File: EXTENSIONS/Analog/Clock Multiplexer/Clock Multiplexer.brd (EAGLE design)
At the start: 47 x 71 mm, 9 parts

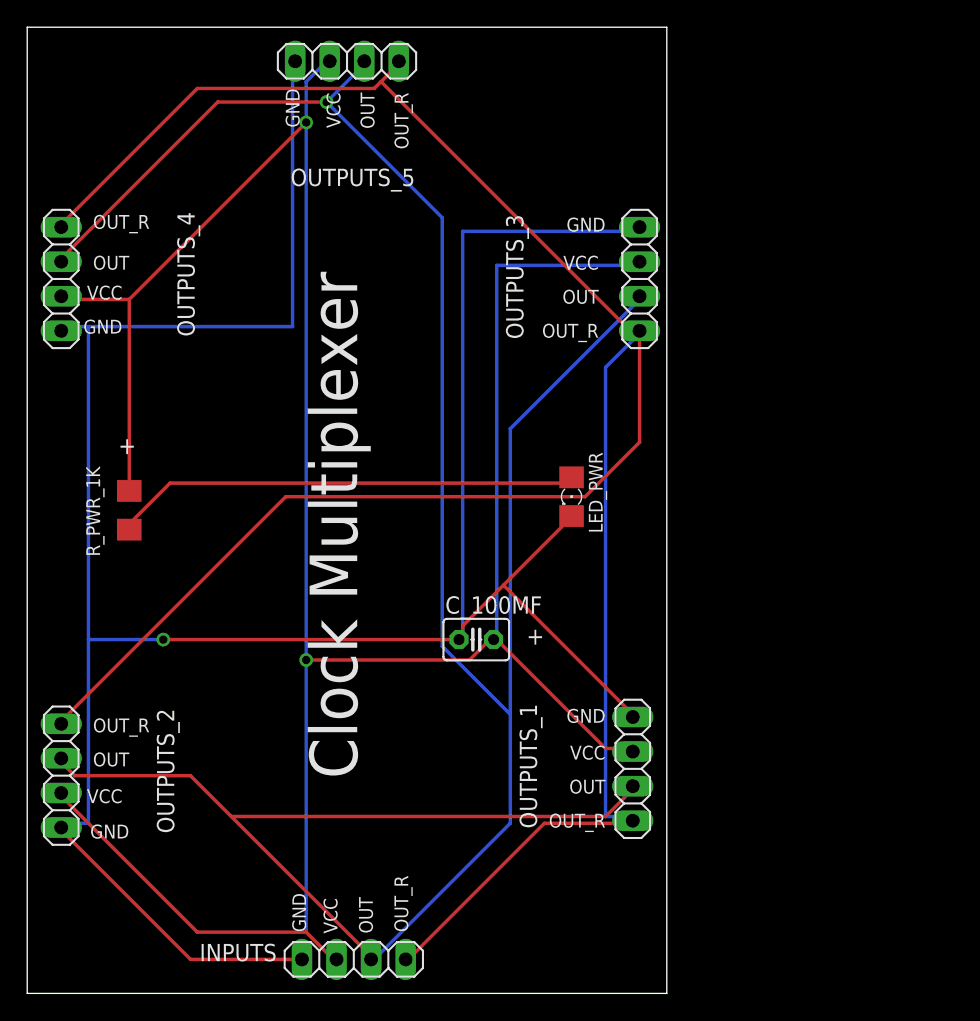
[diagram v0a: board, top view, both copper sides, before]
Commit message: update clock multiplexer
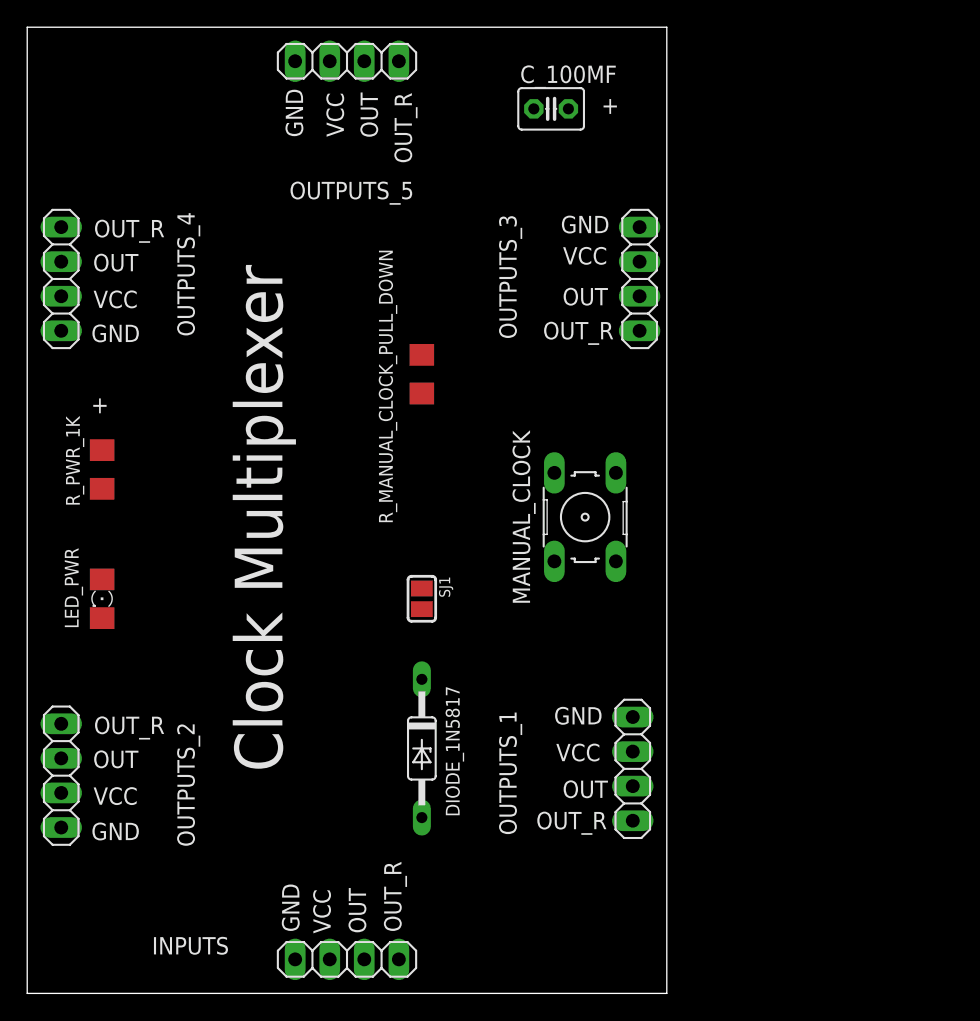
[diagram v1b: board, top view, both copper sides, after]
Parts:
- added DIODE_1N5817: 1N821, diode:DO35Z10
- added MANUAL_CLOCK: (no value), switch-omron:B3F-10XX
- added R_MANUAL_CLOCK_PULL_DOWN: (no value), adafruit:R1206
- added SJ1: (no value), microbuilder:SOLDERJUMPER_REFLOW
- moved C_100MF 39.4 mm to (40.5, 77.0)
- moved LED_PWR 35.3 mm to (7.50, 41.0)
- moved R_PWR_1K 3.61 mm to (7.50, 50.5)
- moved JP_CLOCK_IN 0.50 mm to (25.5, 14.5)
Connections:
- new net N$2: DIODE_1N5817.C, SJ1.2
- new net TMR555_OUTPUT_2: MANUAL_CLOCK.4, OUTPUTS_1.3, OUTPUTS_2.3, OUTPUTS_3.3, OUTPUTS_4.3, OUTPUTS_5.3, R_MANUAL_CLOCK_PULL_DOWN.2, SJ1.1
- net GND: now also R_MANUAL_CLOCK_PULL_DOWN.1
- net TMR555_OUTPUT: now also DIODE_1N5817.A; no longer OUTPUTS_1.3, OUTPUTS_2.3, OUTPUTS_3.3, OUTPUTS_4.3, OUTPUTS_5.3
- net VCC: now also MANUAL_CLOCK.1
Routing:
- net VCC: track 197.7 -> 0.00 mm, vias 2 -> 0
- net TMR555_OUTPUT: track 196.5 -> 0.00 mm, vias 1 -> 0
- net GND: track 194.7 -> 0.00 mm, vias 1 -> 0
- net TMR555_OUTPUT_REVERSE: track 176.5 -> 0.00 mm
- net N$1: track 34.6 -> 0.00 mm
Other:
- board text added: "PCBv1 - 2019.10"
- board text removed: "PCBv1 - 2019.09"

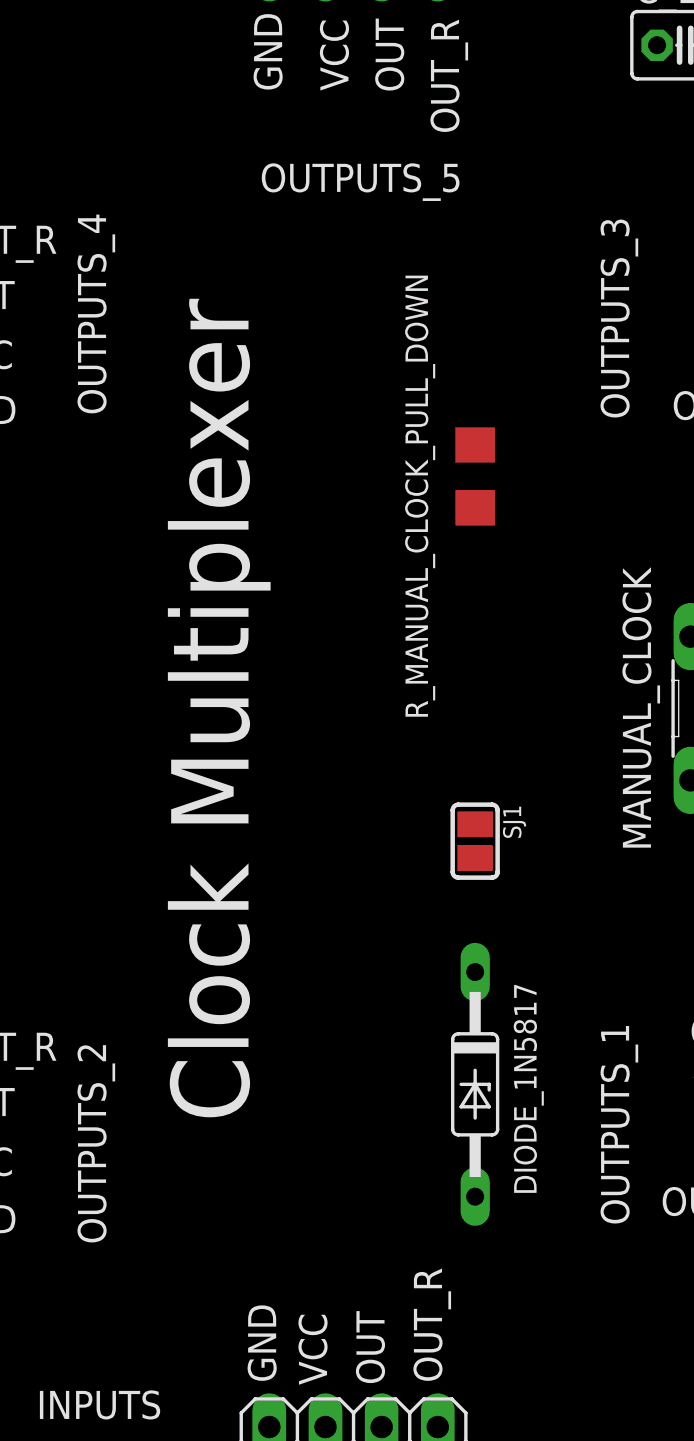
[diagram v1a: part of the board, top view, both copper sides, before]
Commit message: update clock multiplexer
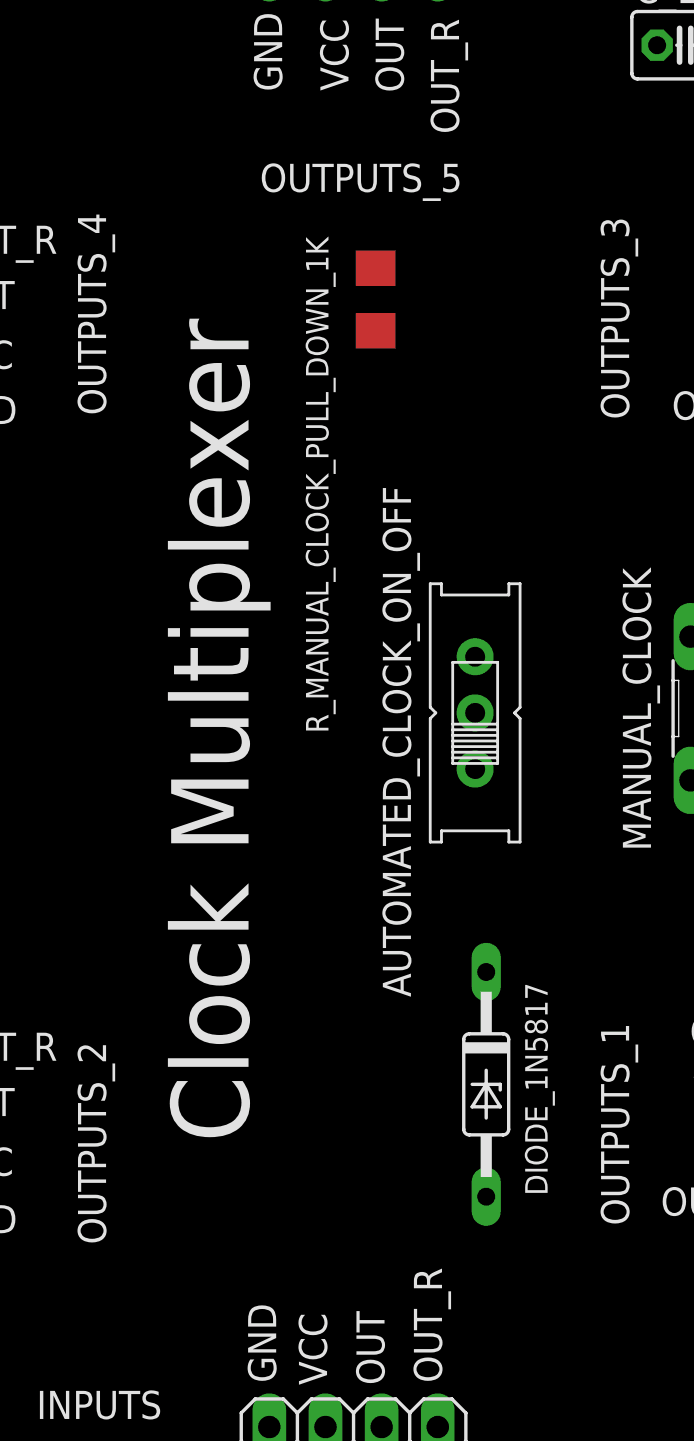
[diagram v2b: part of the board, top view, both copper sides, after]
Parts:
- removed R_MANUAL_CLOCK_PULL_DOWN: (no value), adafruit:R1206
- removed SJ1: (no value), microbuilder:SOLDERJUMPER_REFLOW
- added AUTOMATED_CLOCK_ON_OFF: (no value), adafruit:EG1218
- added R_MANUAL_CLOCK_PULL_DOWN_1K: (no value), adafruit:R1206
- moved DIODE_1N5817 0.50 mm to (31.5, 30.0)
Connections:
- net GND: now also R_MANUAL_CLOCK_PULL_DOWN_1K.1; no longer R_MANUAL_CLOCK_PULL_DOWN.1
- net N$2: now also AUTOMATED_CLOCK_ON_OFF.P; no longer SJ1.2
- net TMR555_OUTPUT_2: now also AUTOMATED_CLOCK_ON_OFF.O, R_MANUAL_CLOCK_PULL_DOWN_1K.2; no longer R_MANUAL_CLOCK_PULL_DOWN.2, SJ1.1
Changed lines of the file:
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@@
 <text x="42" y="24.7" size="1.27" layer="25" rot="R180" align="center">OUT_R</text>
 <text x="27.5" y="21" size="1.27" layer="26" rot="MR0" align="center">PCBv1 - 2019.10</text>
-<text x="19" y="46.9" size="3.5" layer="25" rot="R270" align="center">Clock Multiplexer</text>
+<text x="19" y="46" size="3.5" layer="25" rot="R270" align="center">Clock Multiplexer</text>
 <text x="14" y="15.5" size="1.27" layer="25" rot="R180" align="center">INPUTS</text>
 <text x="27" y="48" size="3.5" layer="26" rot="MR90" align="center">MadeInTheUSB.net</text>
@@
 <attribute name="VALUE" x="48.08" y="43.952" size="1.27" layer="27" ratio="10" rot="R90"/>
 </element>
-<element name="R_MANUAL_CLOCK_PULL_DOWN" library="adafruit" package="R1206" value="" x="31" y="57.5" smashed="yes" rot="R90">
-<attribute name="NAME" x="28.357" y="56.603" size="1.016" layer="25" rot="R90" align="center"/>
-<attribute name="VALUE" x="33.413" y="56.103" size="1.27" layer="27" rot="R90"/>
-</element>
-<element name="SJ1" library="microbuilder" package="SOLDERJUMPER_REFLOW" value="" x="31" y="41" rot="R270"/>
-<element name="DIODE_1N5817" library="diode" package="DO35Z10" value="1N821" x="31" y="30" smashed="yes" rot="R270">
-<attribute name="NAME" x="33.27" y="29.786" size="1.016" layer="25" ratio="10" rot="R270" align="center"/>
-<attribute name="VALUE" x="28.46" y="32.286" size="1.27" layer="27" ratio="10" rot="R270"/>
+<element name="R_MANUAL_CLOCK_PULL_DOWN_1K" library="adafruit" package="R1206" value="" x="26.5" y="65.5" smashed="yes" rot="R90">
+<attribute name="NAME" x="23.857" y="57.103" size="1.016" layer="25" rot="R90" align="center"/>
+<attribute name="VALUE" x="28.913" y="64.103" size="1.27" layer="27" rot="R90"/>
+</element>
+<element name="DIODE_1N5817" library="diode" package="DO35Z10" value="1N821" x="31.5" y="30" smashed="yes" rot="R270">
+<attribute name="NAME" x="33.77" y="29.786" size="1.016" layer="25" ratio="10" rot="R270" align="center"/>
+<attribute name="VALUE" x="28.96" y="32.286" size="1.27" layer="27" ratio="10" rot="R270"/>
+</element>
+<element name="AUTOMATED_CLOCK_ON_OFF" library="adafruit" package="EG1218" value="" x="31" y="46.8" smashed="yes" rot="R90">
+<attribute name="NAME" x="27.46" y="45.506" size="1.27" layer="25" font="vector" rot="R90" align="center"/>
 </element>
 </elements>
@@
 <contactref element="OUTPUTS_5" pad="1"/>
 <contactref element="C_100MF" pad="1"/>
-<contactref element="R_MANUAL_CLOCK_PULL_DOWN" pad="1"/>
+<contactref element="R_MANUAL_CLOCK_PULL_DOWN_1K" pad="1"/>
 <wire x1="47" y1="68.31" x2="39.23" y2="77" width="0" layer="19" extent="1-1"/>
-<wire x1="21.69" y1="80.5" x2="39.23" y2="77" width="0" layer="19" extent="1-1"/>
-<wire x1="4.5" y1="60.69" x2="21.69" y2="80.5" width="0" layer="19" extent="1-1"/>
+<wire x1="26.5" y1="64.078" x2="39.23" y2="77" width="0" layer="19" extent="1-1"/>
+<wire x1="21.69" y1="80.5" x2="26.5" y2="64.078" width="0" layer="19" extent="1-1"/>
+<wire x1="4.5" y1="60.69" x2="26.5" y2="64.078" width="0" layer="19" extent="1-1"/>
 <wire x1="7.5" y1="39.578" x2="4.5" y2="60.69" width="0" layer="19" extent="1-1"/>
 <wire x1="4.5" y1="24.19" x2="7.5" y2="39.578" width="0" layer="19" extent="1-1"/>
 <wire x1="21.69" y1="14.5" x2="4.5" y2="24.19" width="0" layer="19" extent="1-1"/>
-<wire x1="31" y1="56.078" x2="7.5" y2="39.578" width="0" layer="19" extent="1-1"/>
-<wire x1="46.5" y1="32.31" x2="31" y2="56.078" width="0" layer="19" extent="1-1"/>
+<wire x1="46.5" y1="32.31" x2="21.69" y2="14.5" width="0" layer="19" extent="1-1"/>
 </signal>
 <signal name="VCC">
@@
 <contactref element="JP_CLOCK_IN" pad="3"/>
 <contactref element="DIODE_1N5817" pad="A"/>
-<wire x1="26.77" y1="14.5" x2="31" y2="24.92" width="0" layer="19" extent="1-1"/>
+<wire x1="26.77" y1="14.5" x2="31.5" y2="24.92" width="0" layer="19" extent="1-1"/>
 </signal>
 <signal name="TMR555_OUTPUT_REVERSE">
@@
 <contactref element="OUTPUTS_4" pad="3"/>
 <contactref element="MANUAL_CLOCK" pad="4"/>
-<contactref element="R_MANUAL_CLOCK_PULL_DOWN" pad="2"/>
-<contactref element="SJ1" pad="1"/>
+<contactref element="R_MANUAL_CLOCK_PULL_DOWN_1K" pad="2"/>
+<contactref element="AUTOMATED_CLOCK_ON_OFF" pad="O"/>
 <wire x1="45.2606" y1="50.2512" x2="47" y2="63.23" width="0" layer="19" extent="1-1"/>
-<wire x1="31" y1="58.922" x2="45.2606" y2="50.2512" width="0" layer="19" extent="1-1"/>
-<wire x1="31" y1="41.762" x2="31" y2="58.922" width="0" layer="19" extent="1-1"/>
-<wire x1="4.5" y1="29.27" x2="31" y2="41.762" width="0" layer="19" extent="1-1"/>
-<wire x1="46.5" y1="27.23" x2="45.2606" y2="50.2512" width="0" layer="19" extent="1-1"/>
-<wire x1="26.77" y1="80.5" x2="47" y2="63.23" width="0" layer="19" extent="1-1"/>
-<wire x1="4.5" y1="65.77" x2="26.77" y2="80.5" width="0" layer="19" extent="1-1"/>
+<wire x1="31" y1="44.26" x2="45.2606" y2="50.2512" width="0" layer="19" extent="1-1"/>
+<wire x1="26.5" y1="66.922" x2="47" y2="63.23" width="0" layer="19" extent="1-1"/>
+<wire x1="26.77" y1="80.5" x2="26.5" y2="66.922" width="0" layer="19" extent="1-1"/>
+<wire x1="4.5" y1="65.77" x2="26.5" y2="66.922" width="0" layer="19" extent="1-1"/>
+<wire x1="46.5" y1="27.23" x2="31" y2="44.26" width="0" layer="19" extent="1-1"/>
+<wire x1="4.5" y1="29.27" x2="31" y2="44.26" width="0" layer="19" extent="1-1"/>
 </signal>
 <signal name="N$2">
 <contactref element="DIODE_1N5817" pad="C"/>
-<contactref element="SJ1" pad="2"/>
-<wire x1="31" y1="40.238" x2="31" y2="35.08" width="0" layer="19" extent="1-1"/>
+<contactref element="AUTOMATED_CLOCK_ON_OFF" pad="P"/>
+<wire x1="31.5" y1="35.08" x2="31" y2="46.8" width="0" layer="19" extent="1-1"/>
 </signal>
 </signals>

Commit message: update clock multiplexer
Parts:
- turned LED_PWR to 90 degrees
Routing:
- net VCC: track 0.00 -> 189.0 mm, vias 0 -> 1
- net GND: track 0.00 -> 159.8 mm
- net TMR555_OUTPUT_2: track 0.00 -> 149.0 mm, vias 0 -> 2
- net TMR555_OUTPUT_REVERSE: track 0.00 -> 147.3 mm, vias 0 -> 1
- net TMR555_OUTPUT: track 0.00 -> 12.5 mm
- net N$2: track 0.00 -> 12.5 mm
- net N$1: track 0.00 -> 10.6 mm

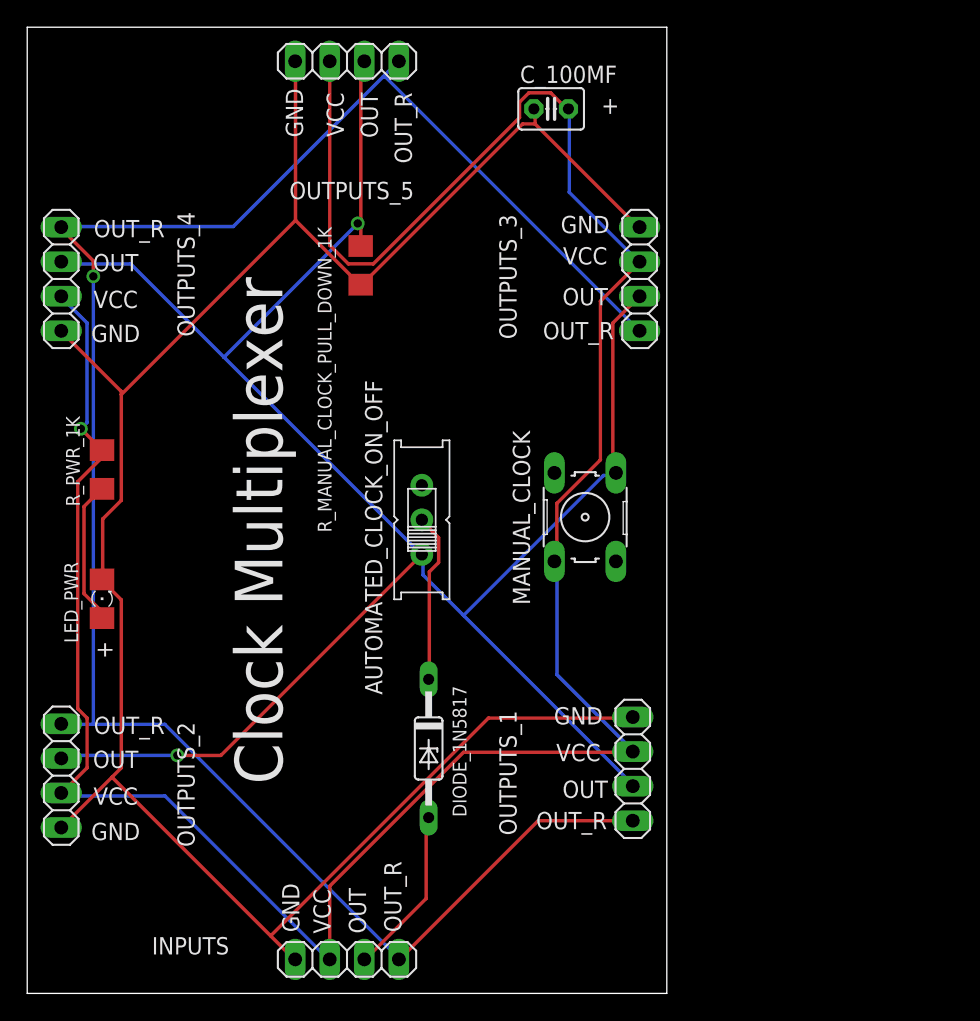
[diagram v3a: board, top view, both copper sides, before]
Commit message: Create v2 of Clock de-multiplexer
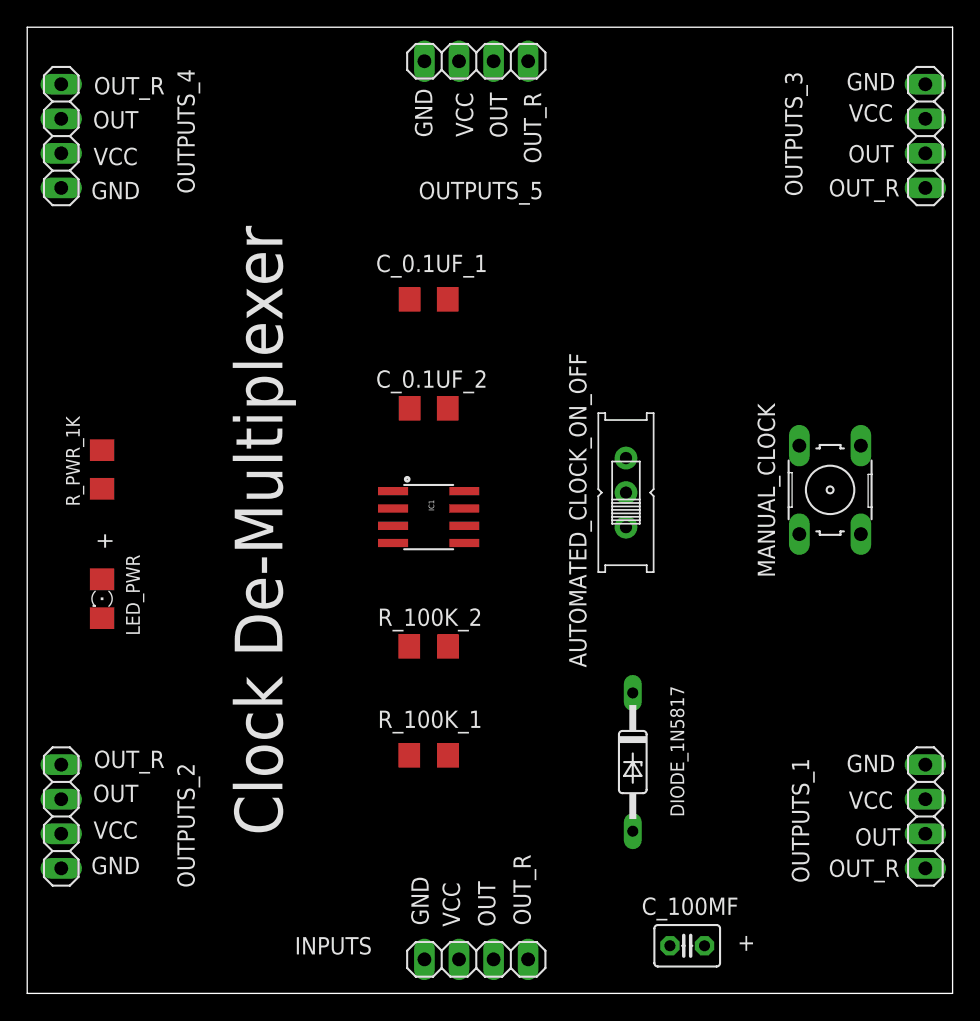
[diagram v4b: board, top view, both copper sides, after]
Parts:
- removed R_MANUAL_CLOCK_PULL_DOWN_1K: (no value), adafruit:R1206
- added C_0.1UF_1, C_0.1UF_2: (no value), adafruit:C1206
- added IC1: (no value), SparkFun-AnalogIC:SO08
- added R_100K_1, R_100K_2: (no value), adafruit:R1206
- moved C_100MF 62.3 mm to (50.5, 15.5)
- moved OUTPUTS_3 23.5 mm to (68.0, 75.0)
- moved OUTPUTS_1 21.8 mm to (68.0, 25.0)
- moved MANUAL_CLOCK 18.1 mm to (61.0, 49.0)
- moved AUTOMATED_CLOCK_ON_OFF 15.1 mm to (46.0, 48.8)
- moved DIODE_1N5817 15.0 mm to (46.5, 29.0)
- moved OUTPUTS_4 10.5 mm to (4.50, 75.0)
- moved JP_CLOCK_IN 9.50 mm to (35.0, 14.5)
- moved OUTPUTS_5 9.50 mm to (35.0, 80.5)
- moved OUTPUTS_2 3.00 mm to (4.50, 25.0)
- turned LED_PWR to 270 degrees
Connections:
- new net N$3: C_0.1UF_1.2, IC1.6, IC1.7, R_100K_1.2
- new net N$4: C_0.1UF_2.2, IC1.5
- new net N$5: IC1.2, MANUAL_CLOCK.1, R_100K_2.2
- net GND: now also C_0.1UF_1.1, C_0.1UF_2.1, IC1.1, MANUAL_CLOCK.4; no longer R_MANUAL_CLOCK_PULL_DOWN_1K.1
- net TMR555_OUTPUT_2: now also IC1.3; no longer MANUAL_CLOCK.4, R_MANUAL_CLOCK_PULL_DOWN_1K.2
- net VCC: now also IC1.4, IC1.8, R_100K_1.1, R_100K_2.1; no longer MANUAL_CLOCK.1
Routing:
- net VCC: track 189.0 -> 0.00 mm, vias 1 -> 0
- net GND: track 159.8 -> 0.00 mm
- net TMR555_OUTPUT_2: track 149.0 -> 0.00 mm, vias 2 -> 0
- net TMR555_OUTPUT_REVERSE: track 147.3 -> 0.00 mm, vias 1 -> 0
- net TMR555_OUTPUT: track 12.5 -> 0.00 mm
- net N$2: track 12.5 -> 0.00 mm
- net N$1: track 10.6 -> 0.00 mm
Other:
- board size 47 x 71 mm -> 68 x 71 mm
- board text added: "Clock De-Multiplexer"
- board text added: "PCBv2 - 2019.12"
- board text added: "www.FredericTorres.com"
- board text removed: "Clock Multiplexer"
- board text removed: "PCBv1 - 2019.10"
